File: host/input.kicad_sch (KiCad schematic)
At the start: 21 parts, among them J2 Conn_01x04, J4 Conn_01x06, U1 PCA9615DP

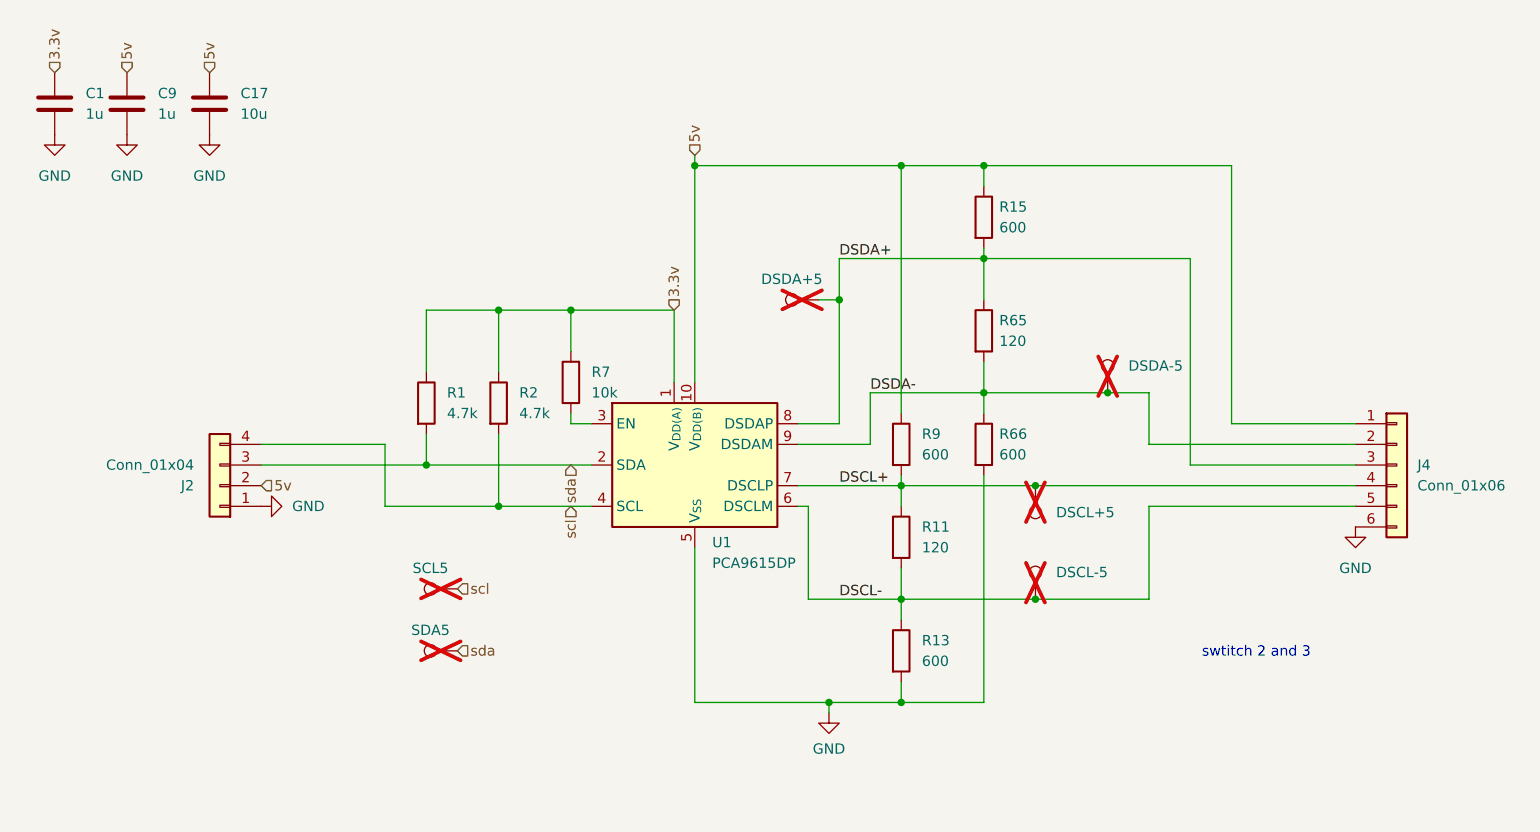
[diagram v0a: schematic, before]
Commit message: updated host schematic and imu production files
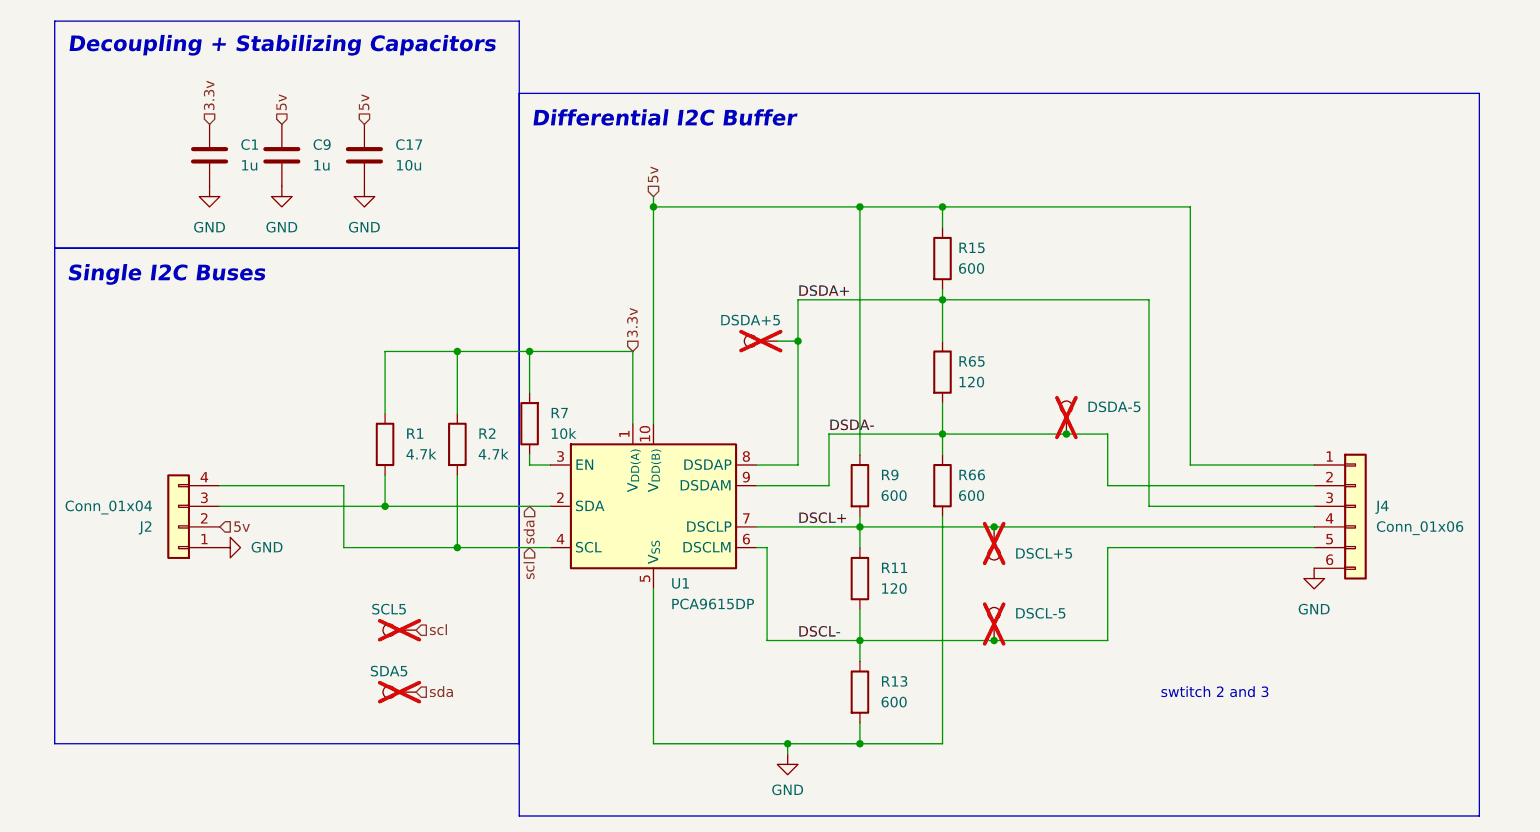
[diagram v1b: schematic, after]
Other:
- note added: "Decoupling + Stabilizing Capacitors"
- note added: "Differential I2C Buffer"
- note added: "Single I2C Buses"
- moved on the sheet: C1, C17, C9, DSCL+5, DSCL-5, DSDA+5, DSDA-5, J2, J4, R1, R11, R13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
